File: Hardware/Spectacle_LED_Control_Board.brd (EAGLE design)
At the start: 25.4 x 55.9 mm, 39 parts, among them J1 FTDI_DEVICE, J3 USB-MICROB, J4 AUDIO-JACK3, J8 AUDIO-JACK3, U1 CY8C4146LQI-S422, U2 3.3V/150mA

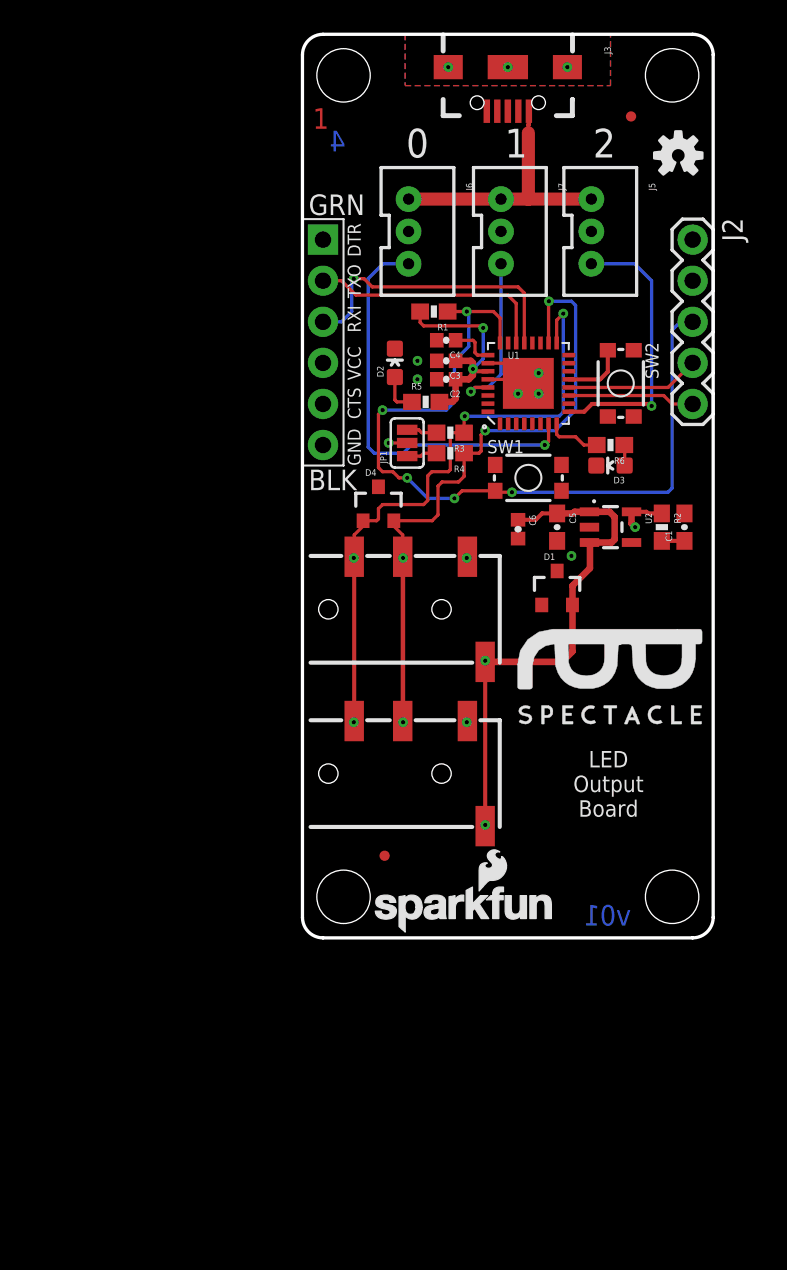
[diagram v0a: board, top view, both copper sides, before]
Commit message: Added circuitry for downstream power control
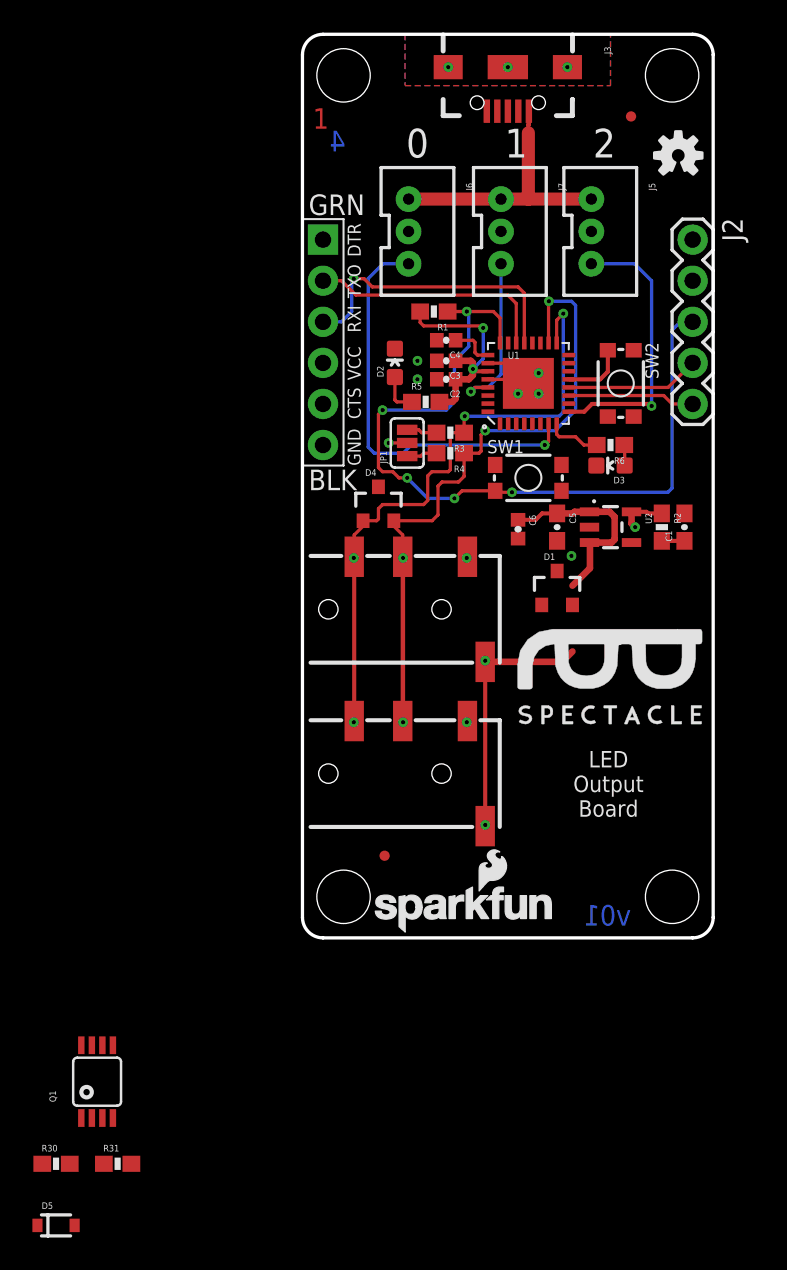
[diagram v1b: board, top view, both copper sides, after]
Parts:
- added D5: BAT20J, SparkFun-DiscreteSemi:SOD-323
- added Q1: (no value), SparkFun-DiscreteSemi:MSOP8
- added R30, R31: 10K, SparkFun-Resistors:0603-RES
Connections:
- new net N$26: Q1.4, Q1.7, Q1.8, R31.1
- new net VOUT: D1.2, J8.EARTH, Q1.5, Q1.6
- new net V_OUT_EN: Q1.2, R30.1
- net 5V: now also D5.C
- net GND: now also Q1.1, R30.2
- net VIN: now also D1.1, D5.A, Q1.3, R31.2; no longer D1.2, J8.EARTH
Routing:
- net VIN: track 33.6 -> 28.9 mm
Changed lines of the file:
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@@
 <layer number="46" name="Milling" color="3" fill="1" visible="no" active="yes"/>
 <layer number="47" name="Measures" color="7" fill="1" visible="no" active="yes"/>
+<layer number="48" name="Document" color="7" fill="1" visible="no" active="yes"/>
+<layer number="49" name="Reference" color="7" fill="1" visible="no" active="yes"/>
 <layer number="51" name="tDocu" color="6" fill="1" visible="yes" active="yes"/>
 <layer number="52" name="bDocu" color="7" fill="1" visible="no" active="yes"/>
-<layer number="48" name="Document" color="7" fill="1" visible="no" active="no"/>
-<layer number="49" name="Reference" color="7" fill="1" visible="no" active="no"/>
 <layer number="3" name="Route3" color="4" fill="3" visible="no" active="no"/>
 <layer number="4" name="Route4" color="1" fill="4" visible="no" active="no"/>
@@
 <element name="FD1" library="SparkFun-Aesthetics" package="MICRO-FIDUCIAL" value="FIDUCIALUFIDUCIAL" x="5.08" y="5.08"/>
 <element name="FD2" library="SparkFun-Aesthetics" package="MICRO-FIDUCIAL" value="FIDUCIALUFIDUCIAL" x="20.32" y="50.8"/>
+<element name="Q1" library="SparkFun-DiscreteSemi" package="MSOP8" value="" x="-12.7" y="-8.89">
+<attribute name="PROD_ID" value="TRANS-07913" x="-12.7" y="-8.89" size="1.778" layer="27" font="vector" ratio="15" display="off"/>
+</element>
+<element name="R30" library="SparkFun-Resistors" package="0603-RES" value="10K" x="-15.24" y="-13.97">
+<attribute name="PROD_ID" value="RES-00824" x="-15.24" y="-13.97" size="1.778" layer="27" font="vector" ratio="15" display="off"/>
+</element>
+<element name="R31" library="SparkFun-Resistors" package="0603-RES" value="10K" x="-11.43" y="-13.97">
+<attribute name="PROD_ID" value="RES-00824" x="-15.24" y="-17.78" size="1.778" layer="27" font="vector" ratio="15" display="off"/>
+</element>
+<element name="D5" library="SparkFun-DiscreteSemi" package="SOD-323" value="BAT20J" x="-15.24" y="-17.78">
+<attribute name="PROD_ID" value="DIO-11623" x="-19.05" y="-12.7" size="1.778" layer="27" font="vector" ratio="15" display="off"/>
+</element>
 </elements>
 <signals>
@@
 <via x="10.16" y="13.335" extent="1-16" drill="0.254"/>
 <via x="10.16" y="23.495" extent="1-16" drill="0.254"/>
+<contactref element="Q1" pad="1"/>
+<contactref element="R30" pad="2"/>
+<wire x1="17.865" y1="43.688" x2="24.13" y2="40.64" width="0" layer="19" extent="1-1"/>
+<wire x1="12.277" y1="43.688" x2="17.865" y2="43.688" width="0" layer="19" extent="1-1"/>
+<wire x1="6.562" y1="43.688" x2="12.277" y2="43.688" width="0" layer="19" extent="1-1"/>
+<wire x1="8.31" y1="36.957" x2="6.562" y2="43.688" width="0" layer="19" extent="1-1"/>
+<wire x1="8.31" y1="35.687" x2="8.31" y2="36.957" width="0" layer="19" extent="1-1"/>
+<wire x1="8.31" y1="34.544" x2="8.31" y2="35.687" width="0" layer="19" extent="1-1"/>
+<wire x1="7.112" y1="35.687" x2="8.31" y2="35.687" width="0" layer="19" extent="1-1"/>
+<wire x1="7.112" y1="34.544" x2="7.112" y2="35.687" width="0" layer="19" extent="1-1"/>
+<wire x1="5.715" y1="36.437" x2="7.112" y2="35.687" width="0" layer="19" extent="1-1"/>
+<wire x1="11.47" y1="35.54" x2="8.31" y2="35.687" width="0" layer="19" extent="1-1"/>
+<wire x1="14.605" y1="33.655" x2="13.97" y2="34.29" width="0" layer="19" extent="1-1"/>
+<wire x1="13.335" y1="33.655" x2="13.97" y2="34.29" width="0" layer="19" extent="1-1"/>
+<wire x1="16.02" y1="29.248" x2="14.605" y2="33.655" width="0" layer="19" extent="1-1"/>
+<wire x1="18.173" y1="29.21" x2="16.02" y2="29.248" width="0" layer="19" extent="1-1"/>
+<wire x1="20.485" y1="32.24" x2="18.173" y2="29.21" width="0" layer="19" extent="1-1"/>
+<wire x1="17.7499" y1="25.4" x2="18.173" y2="29.21" width="0" layer="19" extent="1-1"/>
+<wire x1="16.637" y1="23.622" x2="17.7499" y2="25.4" width="0" layer="19" extent="1-1"/>
+<wire x1="15.748" y1="24.55" x2="16.637" y2="23.622" width="0" layer="19" extent="1-1"/>
+<wire x1="15.748" y1="22.69" x2="16.637" y2="23.622" width="0" layer="19" extent="1-1"/>
+<wire x1="13.335" y1="24.693" x2="15.748" y2="24.55" width="0" layer="19" extent="1-1"/>
+<wire x1="10.2" y1="23.57" x2="13.335" y2="24.693" width="0" layer="19" extent="1-1"/>
+<wire x1="10.16" y1="23.495" x2="10.2" y2="23.57" width="0" layer="19" extent="1-1"/>
+<wire x1="1.27" y1="33.02" x2="5.715" y2="36.437" width="0" layer="19" extent="1-1"/>
+<wire x1="1.27" y1="30.48" x2="1.27" y2="33.02" width="0" layer="19" extent="1-1"/>
+<wire x1="4.699" y1="27.897" x2="1.27" y2="30.48" width="0" layer="19" extent="1-1"/>
+<wire x1="23.622" y1="26.25" x2="17.7499" y2="25.4" width="0" layer="19" extent="1-1"/>
+<wire x1="11.4" y1="51.123" x2="12.277" y2="43.688" width="0" layer="19" extent="1-1"/>
+<wire x1="10.2" y1="13.41" x2="10.16" y2="23.495" width="0" layer="19" extent="1-1"/>
+<wire x1="10.16" y1="13.335" x2="10.2" y2="13.41" width="0" layer="19" extent="1-1"/>
+<wire x1="-13.675" y1="-11.14" x2="10.16" y2="13.335" width="0" layer="19" extent="1-1"/>
+<wire x1="-14.39" y1="-13.97" x2="-13.675" y2="-11.14" width="0" layer="19" extent="1-1"/>
 </signal>
 <signal name="VCC">
@@
 <wire x1="16.725" y1="26.25" x2="16.825" y2="26.35" width="0.4064" layer="1"/>
 <wire x1="16.825" y1="26.35" x2="17.7499" y2="26.35" width="0.4064" layer="1"/>
-<contactref element="D1" pad="2"/>
 <wire x1="17.78" y1="24.4199" x2="17.7499" y2="24.45" width="0.4064" layer="1"/>
 <wire x1="17.7499" y1="24.45" x2="19.116" y2="24.45" width="0.4064" layer="1"/>
@@
 <wire x1="18.989" y1="26.35" x2="17.7499" y2="26.35" width="0.4064" layer="1"/>
 <wire x1="11.3" y1="17.07" x2="16.054" y2="17.07" width="0.4064" layer="1"/>
-<contactref element="J8" pad="EARTH"/>
 <wire x1="11.3" y1="17.07" x2="11.3" y2="16.51" width="0.254" layer="1"/>
 <wire x1="11.3" y1="16.51" x2="11.3" y2="7.62" width="0.254" layer="1"/>
-<wire x1="11.3" y1="7.62" x2="11.3" y2="6.91" width="0.254" layer="1"/>
-<wire x1="16.698" y1="20.59" x2="16.698" y2="17.714" width="0.4064" layer="1"/>
 <wire x1="16.698" y1="17.714" x2="16.054" y2="17.07" width="0.4064" layer="1"/>
 <wire x1="17.78" y1="24.4199" x2="17.78" y2="22.86" width="0.4064" layer="1"/>
 <wire x1="17.78" y1="22.86" x2="16.698" y2="21.778" width="0.4064" layer="1"/>
-<wire x1="16.698" y1="20.59" x2="16.698" y2="21.778" width="0.4064" layer="1"/>
 <via x="11.303" y="6.985" extent="1-16" drill="0.254"/>
 <via x="11.303" y="17.145" extent="1-16" drill="0.254"/>
@@
 <wire x1="15.748" y1="26.25" x2="14.82" y2="26.25" width="0.254" layer="1"/>
 <wire x1="14.82" y1="26.25" x2="14.423" y2="25.853" width="0.254" layer="1"/>
+<contactref element="Q1" pad="3"/>
+<contactref element="R31" pad="2"/>
+<contactref element="D5" pad="A"/>
+<contactref element="D1" pad="1"/>
+<wire x1="14.798" y1="20.59" x2="16.698" y2="21.778" width="0" layer="19" extent="1-1"/>
+<wire x1="16.698" y1="17.714" x2="14.798" y2="20.59" width="0" layer="19" extent="1-1"/>
+<wire x1="-12.375" y1="-11.14" x2="11.303" y2="6.985" width="0" layer="19" extent="1-1"/>
+<wire x1="-10.58" y1="-13.97" x2="-12.375" y2="-11.14" width="0" layer="19" extent="1-1"/>
+<wire x1="-14.09" y1="-17.78" x2="-10.58" y2="-13.97" width="0" layer="19" extent="1-1"/>
 </signal>
 <signal name="N$2">
@@
 <wire x1="13.97" y1="45.688" x2="12.277" y2="45.688" width="0.8128" layer="1"/>
 <wire x1="13.97" y1="49.784" x2="13.97" y2="45.688" width="0.8128" layer="1"/>
+<contactref element="D5" pad="C"/>
+<wire x1="-16.39" y1="-17.78" x2="6.562" y2="45.688" width="0" layer="19" extent="1-1"/>
 </signal>
 <signal name="LED_0">
@@
 <wire x1="10.672" y1="34.04" x2="10.414" y2="33.782" width="0.2032" layer="16"/>
 </signal>
+<signal name="N$26">
+<contactref element="Q1" pad="4"/>
+<contactref element="Q1" pad="8"/>
+<contactref element="Q1" pad="7"/>
+<contactref element="R31" pad="1"/>
+<wire x1="-11.725" y1="-11.14" x2="-12.28" y2="-13.97" width="0" layer="19" extent="1-1"/>
+<wire x1="-13.025" y1="-6.64" x2="-11.725" y2="-11.14" width="0" layer="19" extent="1-1"/>
+<wire x1="-13.675" y1="-6.64" x2="-13.025" y2="-6.64" width="0" layer="19" extent="1-1"/>
+</signal>
+<signal name="VOUT">
+<contactref element="Q1" pad="5"/>
+<contactref element="Q1" pad="6"/>
+<contactref element="D1" pad="2"/>
+<contactref element="J8" pad="EARTH"/>
+<wire x1="11.3" y1="6.91" x2="16.698" y2="20.59" width="0" layer="19" extent="1-1"/>
+<wire x1="-11.725" y1="-6.64" x2="11.3" y2="6.91" width="0" layer="19" extent="1-1"/>
+<wire x1="-12.375" y1="-6.64" x2="-11.725" y2="-6.64" width="0" layer="19" extent="1-1"/>
+</signal>
+<signal name="V_OUT_EN">
+<contactref element="Q1" pad="2"/>
+<contactref element="R30" pad="1"/>
+<wire x1="-13.025" y1="-11.14" x2="-16.09" y2="-13.97" width="0" layer="19" extent="1-1"/>
+</signal>
 </signals>

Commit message: Added enable pin
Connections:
- net V_OUT_EN: now also U1.5
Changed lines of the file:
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@@
 <contactref element="Q1" pad="2"/>
 <contactref element="R30" pad="1"/>
-<wire x1="-13.025" y1="-11.14" x2="-16.09" y2="-13.97" width="0" layer="19" extent="1-1"/>
+<contactref element="U1" pad="5"/>
+<wire x1="-13.025" y1="-11.14" x2="14.22" y2="31.79" width="0" layer="19" extent="1-1"/>
+<wire x1="-16.09" y1="-13.97" x2="-13.025" y2="-11.14" width="0" layer="19" extent="1-1"/>
 </signal>
 </signals>

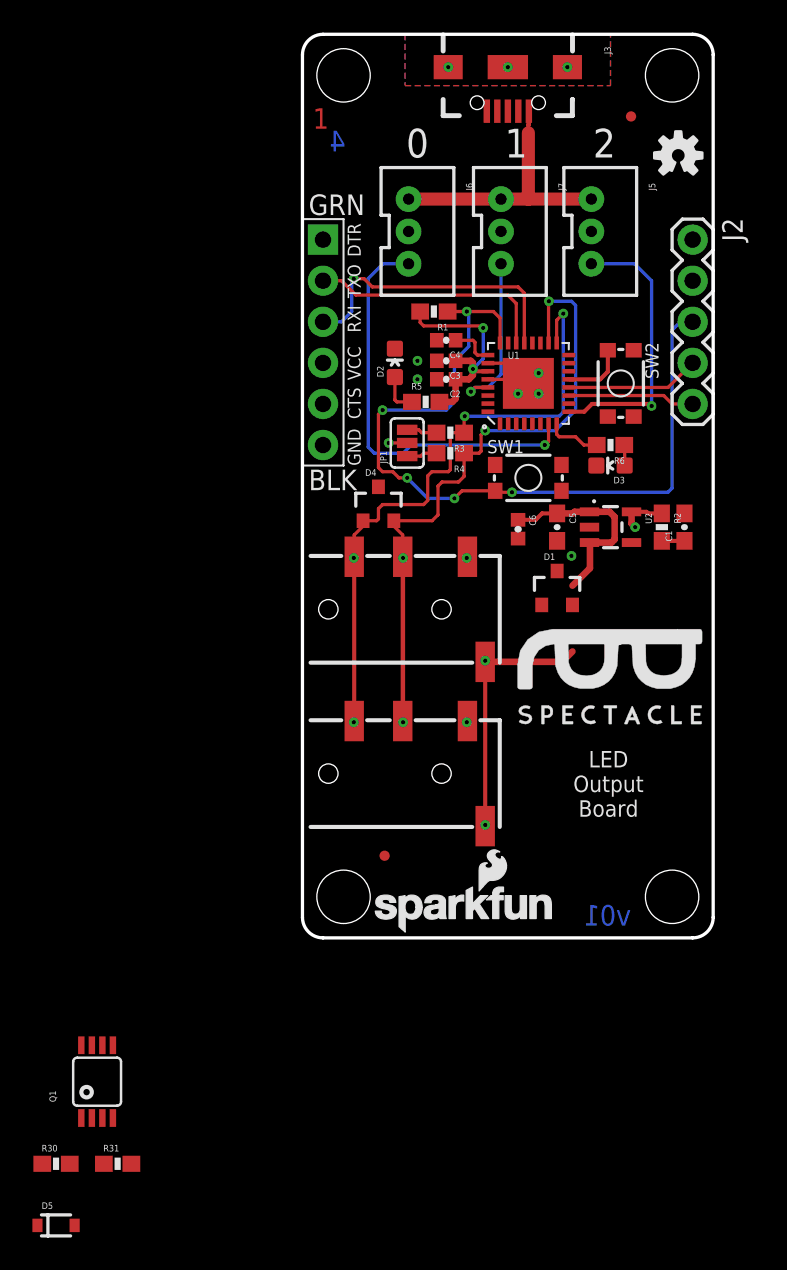
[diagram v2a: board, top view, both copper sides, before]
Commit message: Routed downstream power control
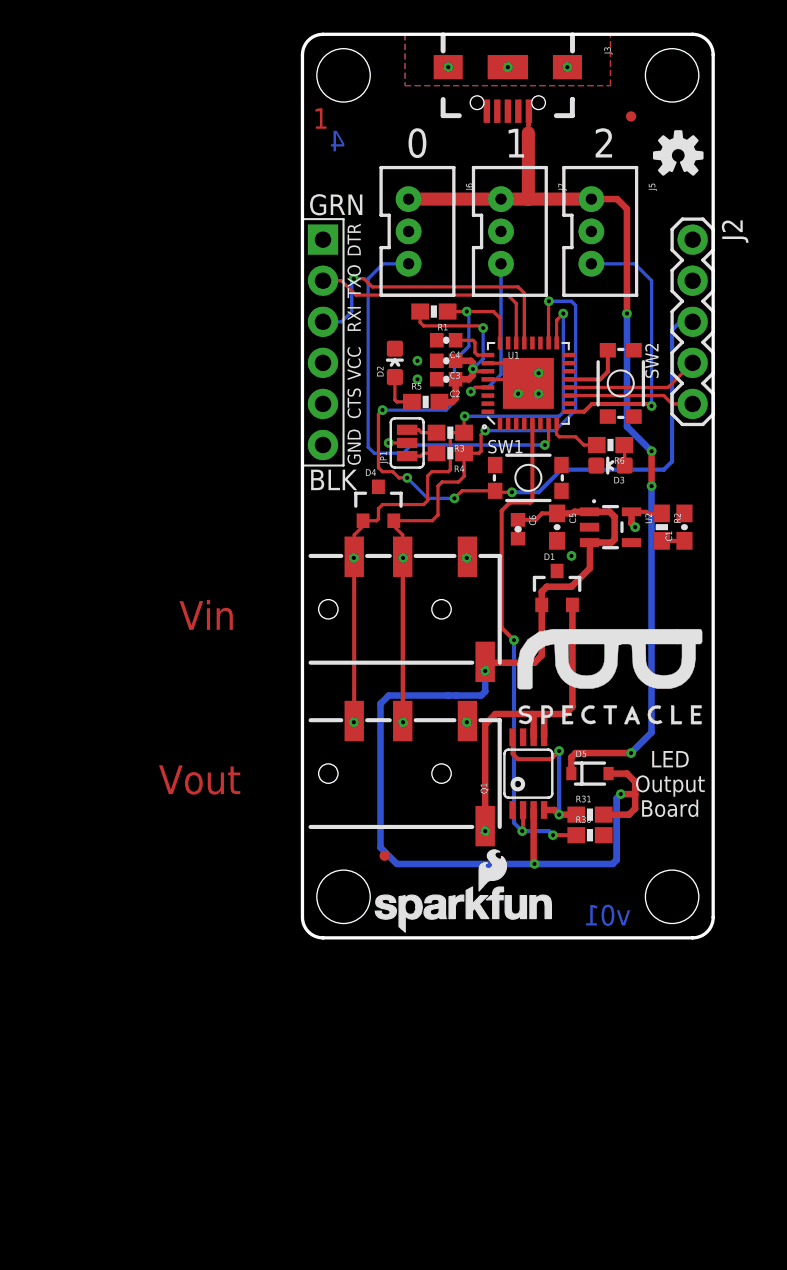
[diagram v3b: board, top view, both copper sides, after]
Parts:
- moved D5 43.3 mm to (17.8, 10.2)
- moved R30 38.8 mm to (17.8, 6.35)
- moved R31 36.3 mm to (17.8, 7.62)
- moved Q1 32.8 mm to (14.0, 10.2)
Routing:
- net 5V: track 16.8 -> 58.8 mm, vias 0 -> 4
- net VIN: track 28.9 -> 69.5 mm, vias 2 -> 3
- net V_OUT_EN: track 0.00 -> 32.0 mm, vias 0 -> 3
- net VOUT: track 0.00 -> 21.7 mm, vias 0 -> 1
- net N$26: track 0.00 -> 10.3 mm, vias 0 -> 2
- net XRES: track 49.8 -> 48.9 mm
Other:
- board text added: "Vin"
- board text added: "Vout"

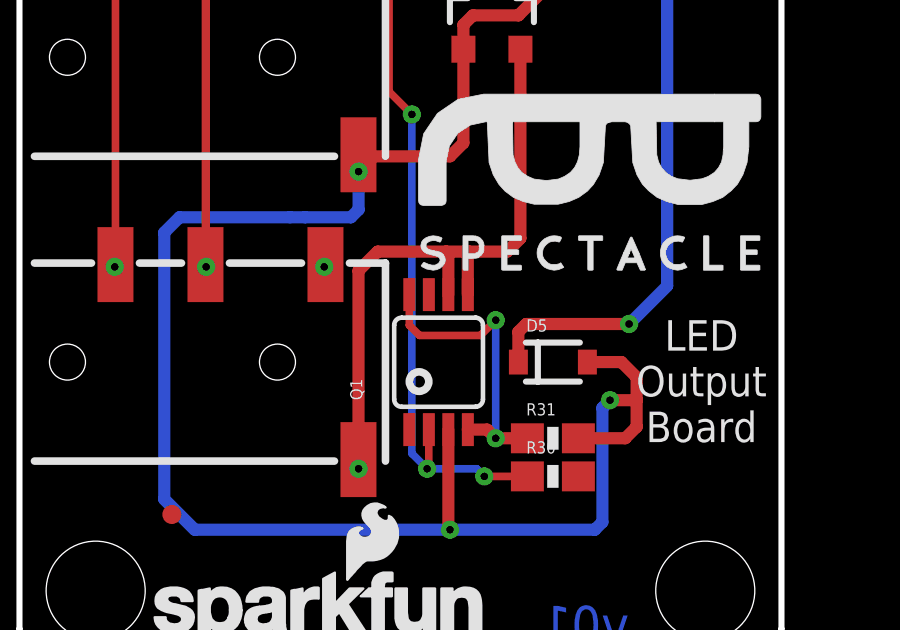
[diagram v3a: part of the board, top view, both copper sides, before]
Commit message: airwire fix
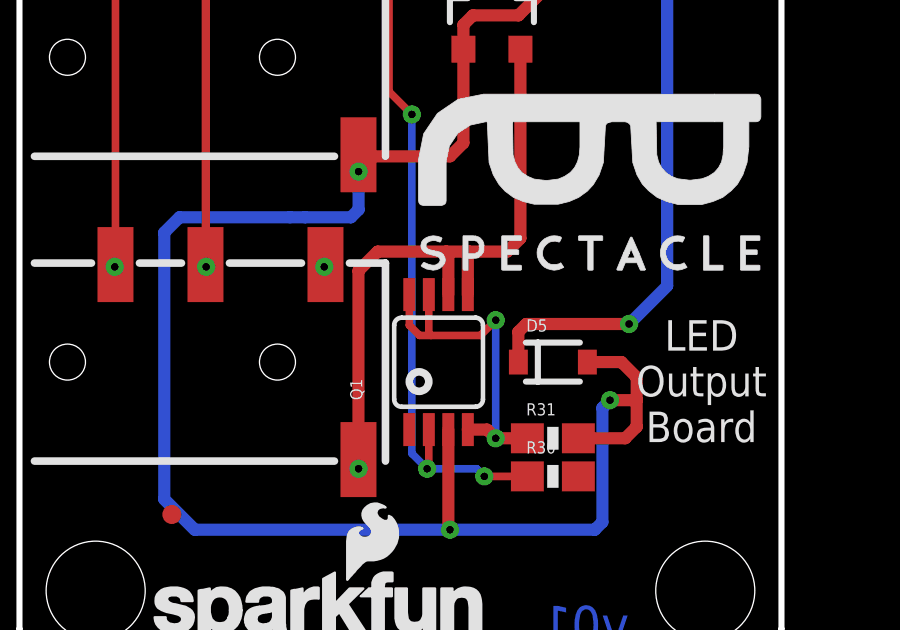
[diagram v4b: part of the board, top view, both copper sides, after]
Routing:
- net N$26: track 10.3 -> 11.7 mm
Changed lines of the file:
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@@
 <wire x1="12.995" y1="12.41" x2="12.995" y2="11.389" width="0.254" layer="1"/>
 <wire x1="12.995" y1="11.389" x2="13.335" y2="11.049" width="0.254" layer="1"/>
-<wire x1="13.335" y1="11.049" x2="15.367" y2="11.049" width="0.254" layer="1"/>
+<wire x1="13.335" y1="11.049" x2="13.716" y2="11.049" width="0.254" layer="1"/>
+<wire x1="13.716" y1="11.049" x2="15.367" y2="11.049" width="0.254" layer="1"/>
 <wire x1="15.367" y1="11.049" x2="15.875" y2="11.557" width="0.254" layer="1"/>
 <via x="15.875" y="11.557" extent="1-16" drill="0.254"/>
@@
 <wire x1="15.585" y1="7.91" x2="15.875" y2="7.62" width="0.4064" layer="1"/>
 <wire x1="16.93" y1="7.62" x2="15.875" y2="7.62" width="0.4064" layer="1"/>
-<wire x1="12.995" y1="12.41" x2="13.645" y2="12.41" width="0" layer="19" extent="1-1"/>
+<wire x1="13.645" y1="12.41" x2="13.645" y2="11.12" width="0.254" layer="1"/>
+<wire x1="13.645" y1="11.12" x2="13.716" y2="11.049" width="0.254" layer="1"/>
 </signal>
 <signal name="VOUT">
